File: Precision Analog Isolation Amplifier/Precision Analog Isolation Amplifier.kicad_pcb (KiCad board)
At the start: 2 copper layers, 33 parts, among them J1 Conn_01x03, J2 Conn_01x03, J3 Conn_Coaxial, J4 Conn_Coaxial

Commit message: Update Schematic & PCB
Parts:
- added C19: 0.1uF, Capacitor_SMD:C_0805_2012Metric_Pad1.18x1.45mm_HandSolder, F.Cu at (163.4, 94.2)
- added C20: 0.1uF, Capacitor_SMD:C_0805_2012Metric_Pad1.18x1.45mm_HandSolder, F.Cu at (167.6, 94.2)
- added D1: ---, Diode_SMD:D_0805_2012Metric_Pad1.15x1.40mm_HandSolder, F.Cu at (159.1, 94.1)
- added G***: LOGO, NaMi_logo:NaMi_logo, F.Cu at (124.9, 101.7)
- added IC1: ADA4899-1YRDZ, ADA4899:SOIC127P600X175-9N, F.Cu at (165.5, 90.3)
- added Q1: ---, Package_TO_SOT_SMD:SOT-23_Handsoldering, F.Cu at (154.9, 83.2)
- added R7: 50R, Resistor_SMD:R_0805_2012Metric_Pad1.20x1.40mm_HandSolder, F.Cu at (160.0, 100.3)
- added REF**: MountingHole_2.2mm_M2_Pad_Via, MountingHole:MountingHole_2.2mm_M2_Pad_Via, F.Cu at (125.6, 76.5)
- added REF**: MountingHole_2.2mm_M2_Pad_Via, MountingHole:MountingHole_2.2mm_M2_Pad_Via, F.Cu at (175.5, 111.5)
- added REF**: MountingHole_2.2mm_M2_Pad_Via, MountingHole:MountingHole_2.2mm_M2_Pad_Via, F.Cu at (175.4, 76.6)
- added REF**: MountingHole_2.2mm_M2_Pad_Via, MountingHole:MountingHole_2.2mm_M2_Pad_Via, F.Cu at (125.6, 111.5)
- added U1: HCNR201, HCNR201-300E:HCNR201300E, F.Cu at (149.8, 91.6)
- added U2: ADA4522, ADA4522:SOIC127P600X175-8N, F.Cu at (144.7, 101.1)
- added U4: ADA4522, ADA4522:SOIC127P600X175-8N, F.Cu at (136.5, 92.6)
- moved C9 76.9 mm to (162.5, 110.4), turned to 180 degrees
- moved C10 74.4 mm to (162.5, 108.4), turned to 180 degrees
- moved J2 73.4 mm to (152.3, 111.4), turned to -90 degrees
- moved C5 72.3 mm to (162.4, 83.7), turned to 180 degrees
- moved C11 72.1 mm to (162.5, 106.4), turned to 180 degrees
- moved C6 71.2 mm to (162.4, 81.7), turned to 180 degrees
- moved FB2 70.8 mm to (159.0, 79.1)
- moved C7 70.4 mm to (162.4, 79.7), turned to 180 degrees
- moved C12 70.0 mm to (162.5, 104.4), turned to 180 degrees
- moved C8 69.8 mm to (162.5, 77.7), turned to 180 degrees
- moved FB3 69.8 mm to (159.0, 109.1)
- moved R1 67.6 mm to (143.9, 84.0)
- moved J1 66.5 mm to (147.4, 76.7)
- moved R3 64.7 mm to (140.5, 88.6), turned to -90 degrees
- moved C17 61.1 mm to (137.4, 87.7), turned to 0 degrees
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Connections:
- C1 pad 2: Net-(C1-Pad2) -> VCC1 +15V
- C10 pad 2: Net-(C10-Pad2) -> VCC2 +15V
- C11 pad 2: Net-(C10-Pad2) -> VCC2 +15V
- C12 pad 2: Net-(C10-Pad2) -> VCC2 +15V
- C13 pad 2: Net-(C13-Pad2) -> VEE2 -15V
- C14 pad 2: Net-(C13-Pad2) -> VEE2 -15V
- C15 pad 2: Net-(C13-Pad2) -> VEE2 -15V
- C16 pad 2: Net-(C13-Pad2) -> VEE2 -15V
- C18 pad 1: Net-(J4-In) -> Vsep_out
- C2 pad 2: Net-(C1-Pad2) -> VCC1 +15V
- C3 pad 2: Net-(C1-Pad2) -> VCC1 +15V
- C4 pad 2: Net-(C1-Pad2) -> VCC1 +15V
- C5 pad 2: Net-(C5-Pad2) -> VEE1 -15V
- C6 pad 2: Net-(C5-Pad2) -> VEE1 -15V
- C7 pad 2: Net-(C5-Pad2) -> VEE1 -15V
- C8 pad 2: Net-(C5-Pad2) -> VEE1 -15V
- C9 pad 2: Net-(C10-Pad2) -> VCC2 +15V
- FB1 pad 1: VCC1 +15V -> VCC1 IN +15V
- FB1 pad 2: Net-(C1-Pad2) -> VCC1 +15V
- FB2 pad 1: VEE1 -15V -> VEE1 IN -15V
- FB2 pad 2: Net-(C5-Pad2) -> VEE1 -15V
- FB3 pad 1: VCC2 +15V -> VCC2 IN +15V
- FB3 pad 2: Net-(C10-Pad2) -> VCC2 +15V
- FB4 pad 1: VEE2 -15V -> VEE2 IN -15V
- FB4 pad 2: Net-(C13-Pad2) -> VEE2 -15V
- J1 pad 1: VCC1 +15V -> VCC1 IN +15V
- J1 pad 3: VEE1 -15V -> VEE1 IN -15V
- J2 pad 1: VCC2 +15V -> VCC2 IN +15V
- J2 pad 3: VEE2 -15V -> VEE2 IN -15V
- J4 pad 1: Net-(J4-In) -> Vout
- RV1 pad 1: Net-(J4-In) -> Vsep_out
- RV1 pad 2: Net-(J4-In) -> Vsep_out
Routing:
- net GND1: track 0.00 -> 122.1 mm, vias 0 -> 7
- net GND2: track 0.00 -> 118.0 mm, vias 0 -> 4
- net VEE1 -15V: track 0.00 -> 51.3 mm, vias 0 -> 2
- net VCC2 +15V: track 0.00 -> 48.8 mm, vias 0 -> 6
- net VEE2 -15V: track 0.00 -> 43.3 mm, vias 0 -> 2
- net VCC1 +15V: track 0.00 -> 34.9 mm, vias 0 -> 2
- net Net-(U1B-K): track 0.00 -> 33.8 mm, vias 0 -> 2
- net Net-(D1-K): track 0.00 -> 29.6 mm
- net Vsep_out: track 0.00 -> 26.5 mm
- net Net-(U1C-K): track 0.00 -> 21.9 mm, vias 0 -> 2
- net Net-(Q1-B): track 0.00 -> 21.3 mm, vias 0 -> 2
- net Vout: track 0.00 -> 18.4 mm, vias 0 -> 2
- net Net-(R6-Pad2): track 0.00 -> 11.4 mm
- net Net-(IC1-+IN): track 0.00 -> 9.94 mm
- net Net-(J3-In): track 0.00 -> 7.24 mm
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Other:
- board outline added: 56 x 41 mm
- board text added: "Input"
- board text added: "KN NaMi Precision Analog Isolation Amplifier Adam Matysiak Kacper Kowalik"
- board text added: "Output"
- board text added: "Primary power supply input"
- board text added: "Secondary power supply input"

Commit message: Update PCB
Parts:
- removed REF** (x4): MountingHole_2.2mm_M2_Pad_Via, MountingHole:MountingHole_2.2mm_M2_Pad_Via
- added D2: SMAJ15A, Diode_SMD:D_SMA, F.Cu at (102.5, 98.0)
- added D3: SMAJ15A, Diode_SMD:D_SMA, F.Cu at (102.5, 77.5)
- added D4: SMAJ15A, Diode_SMD:D_SMA, F.Cu at (175.1, 97.0)
- added D5: SMAJ15A, Diode_SMD:D_SMA, F.Cu at (175.1, 77.0)
- added D6: LED, Diode_SMD:D_0805_2012Metric_Pad1.15x1.40mm_HandSolder, F.Cu at (105.5, 82.0)
- added D7: LED, Diode_SMD:D_0805_2012Metric_Pad1.15x1.40mm_HandSolder, F.Cu at (105.0, 94.0)
- added D8: LED, Diode_SMD:D_0805_2012Metric_Pad1.15x1.40mm_HandSolder, F.Cu at (172.1, 92.5)
- added D9: LED, Diode_SMD:D_0805_2012Metric_Pad1.15x1.40mm_HandSolder, F.Cu at (172.1, 81.5)
- added F1: Fuse, Resistor_SMD:R_0805_2012Metric_Pad1.20x1.40mm_HandSolder, F.Cu at (101.0, 90.5)
- added F2: Fuse, Resistor_SMD:R_0805_2012Metric_Pad1.20x1.40mm_HandSolder, F.Cu at (101.0, 84.5)
- added F3: Fuse, Resistor_SMD:R_0805_2012Metric_Pad1.20x1.40mm_HandSolder, F.Cu at (176.6, 84.0)
- added F4: Fuse, Resistor_SMD:R_0805_2012Metric_Pad1.20x1.40mm_HandSolder, F.Cu at (176.6, 90.0)
- added R10: 33k, Resistor_SMD:R_0805_2012Metric_Pad1.20x1.40mm_HandSolder, F.Cu at (176.6, 92.5)
- added R11: 33k, Resistor_SMD:R_0805_2012Metric_Pad1.20x1.40mm_HandSolder, F.Cu at (176.6, 81.5)
- added R8: 33k, Resistor_SMD:R_0805_2012Metric_Pad1.20x1.40mm_HandSolder, F.Cu at (101.0, 82.0)
- added R9: 33k, Resistor_SMD:R_0805_2012Metric_Pad1.20x1.40mm_HandSolder, F.Cu at (100.5, 94.0)
- moved C8 55.8 mm to (110.0, 96.5)
- moved FB2 54.6 mm to (105.6, 90.5), turned to 0 degrees
- moved C7 54.5 mm to (110.0, 94.5)
- moved C6 53.6 mm to (110.0, 92.5)
- moved C5 52.9 mm to (110.0, 90.5)
- moved J1 51.5 mm to (96.5, 85.0), turned to 0 degrees
- moved J2 39.5 mm to (181.1, 84.5), turned to 0 degrees
- moved Q1 38.0 mm to (117.0, 85.5)
- moved FB4 36.3 mm to (171.6, 90.0), turned to 180 degrees
- moved FB1 35.5 mm to (105.6, 84.5), turned to 0 degrees
- moved C13 33.1 mm to (167.1, 90.0)
- moved C14 33.1 mm to (167.1, 92.0)
- moved C15 33.1 mm to (167.1, 94.0)
- moved C16 33.0 mm to (167.1, 96.2)
- moved C9 32.7 mm to (167.1, 78.0), turned to 0 degrees
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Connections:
- J1 pad 1: VCC1 IN +15V -> Net-(J1-Pin_1)
- J1 pad 3: VEE1 IN -15V -> Net-(J1-Pin_3)
- J2 pad 1: VCC2 IN +15V -> Net-(J2-Pin_1)
- J2 pad 3: VEE2 IN -15V -> Net-(J2-Pin_3)
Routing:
- net GND2: track 118.0 -> 13.1 mm, vias 4 -> 0
- net GND1: track 122.1 -> 70.1 mm, vias 7 -> 0
- net VEE1 -15V: track 51.3 -> 2.95 mm, vias 2 -> 0
- net VCC2 +15V: track 48.8 -> 12.4 mm, vias 6 -> 0
- net VEE2 -15V: track 43.3 -> 10.9 mm, vias 2 -> 0
- net Net-(C17-Pad2): track 4.42 -> 26.5 mm, vias 0 -> 2
- net Net-(Q1-B): track 21.3 -> 6.60 mm, vias 2 -> 0
- net Net-(D1-K): track 29.6 -> 14.9 mm
- net Vout: track 18.4 -> 7.35 mm, vias 2 -> 0
- net Net-(Q1-E): track 5.03 -> 13.8 mm
- net Net-(U1B-K): track 33.8 -> 25.8 mm
- net Net-(J3-In): track 7.24 -> 0.00 mm
- net VCC1 IN +15V: track 7.00 -> 0.00 mm
- net VCC2 IN +15V: track 6.98 -> 0.00 mm
- net VEE1 IN -15V: track 6.89 -> 0.00 mm
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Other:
- board outline removed
- board text removed: "+15V"
- board text removed: "-15V"
- board text removed: "GND1"
- board text removed: "GND2"
- board text removed: "Input"
- board text removed: "Output"
- board text removed: "Primary power supply input"
- board text removed: "Secondary power supply input"

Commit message: Update PCB layout
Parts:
- added REF**: MountingHole_2.2mm_M2_DIN965_Pad, MountingHole:MountingHole_2.2mm_M2_DIN965_Pad, F.Cu at (171.2, 117.3)
- added REF**: MountingHole_2.2mm_M2_DIN965_Pad, MountingHole:MountingHole_2.2mm_M2_DIN965_Pad, F.Cu at (171.2, 79.3)
- added REF**: MountingHole_2.2mm_M2_DIN965_Pad, MountingHole:MountingHole_2.2mm_M2_DIN965_Pad, F.Cu at (113.7, 79.3)
- added REF**: MountingHole_2.2mm_M2_DIN965_Pad, MountingHole:MountingHole_2.2mm_M2_DIN965_Pad, F.Cu at (113.7, 117.3)
- moved R2 39.3 mm to (132.0, 112.8), turned to 90 degrees
- moved R1 36.3 mm to (130.1, 112.8), turned to 90 degrees
- moved U4 35.1 mm to (135.8, 110.8), turned to -90 degrees
- moved R3 33.4 mm to (128.2, 112.8), turned to -90 degrees
- moved RV1 33.3 mm to (147.3, 109.1), turned to -90 degrees
- moved Q1 26.9 mm to (130.1, 109.0), turned to 0 degrees
- moved R5 26.9 mm to (129.3, 106.2), turned to 0 degrees
- moved D1 24.9 mm to (125.3, 108.2), turned to 180 degrees
- moved C17 23.9 mm to (126.2, 112.8), turned to -90 degrees
- moved R6 22.6 mm to (152.9, 111.0)
- moved D3 20.3 mm to (122.0, 83.0), turned to 180 degrees
- moved R9 20.1 mm to (120.3, 97.3)
- moved C5 20.0 mm to (129.4, 95.1)
- moved C6 20.0 mm to (129.4, 97.1)
- moved C7 20.0 mm to (129.4, 99.1)
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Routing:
- net GND1: track 70.1 -> 0.00 mm
- net VCC1 +15V: track 38.3 -> 0.00 mm
- net Vsep_out: track 28.4 -> 0.00 mm, vias 2 -> 0
- net Net-(C17-Pad2): track 26.5 -> 0.00 mm, vias 2 -> 0
- net Net-(U1B-K): track 25.8 -> 0.00 mm, vias 2 -> 0
- net Net-(U1C-K): track 17.2 -> 0.00 mm
- net Net-(D1-K): track 14.9 -> 0.00 mm
- net Net-(R6-Pad2): track 14.2 -> 0.00 mm
- net Net-(Q1-E): track 13.8 -> 0.00 mm
- net GND2: track 13.1 -> 0.00 mm
- net VCC2 +15V: track 12.4 -> 0.00 mm
- net VEE2 -15V: track 10.9 -> 0.00 mm
- net Net-(IC1-+IN): track 10.0 -> 0.00 mm, vias 2 -> 0
- net Vout: track 7.35 -> 0.00 mm
- net Net-(Q1-B): track 6.60 -> 0.00 mm
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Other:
- board outline added: 63.5 x 44 mm

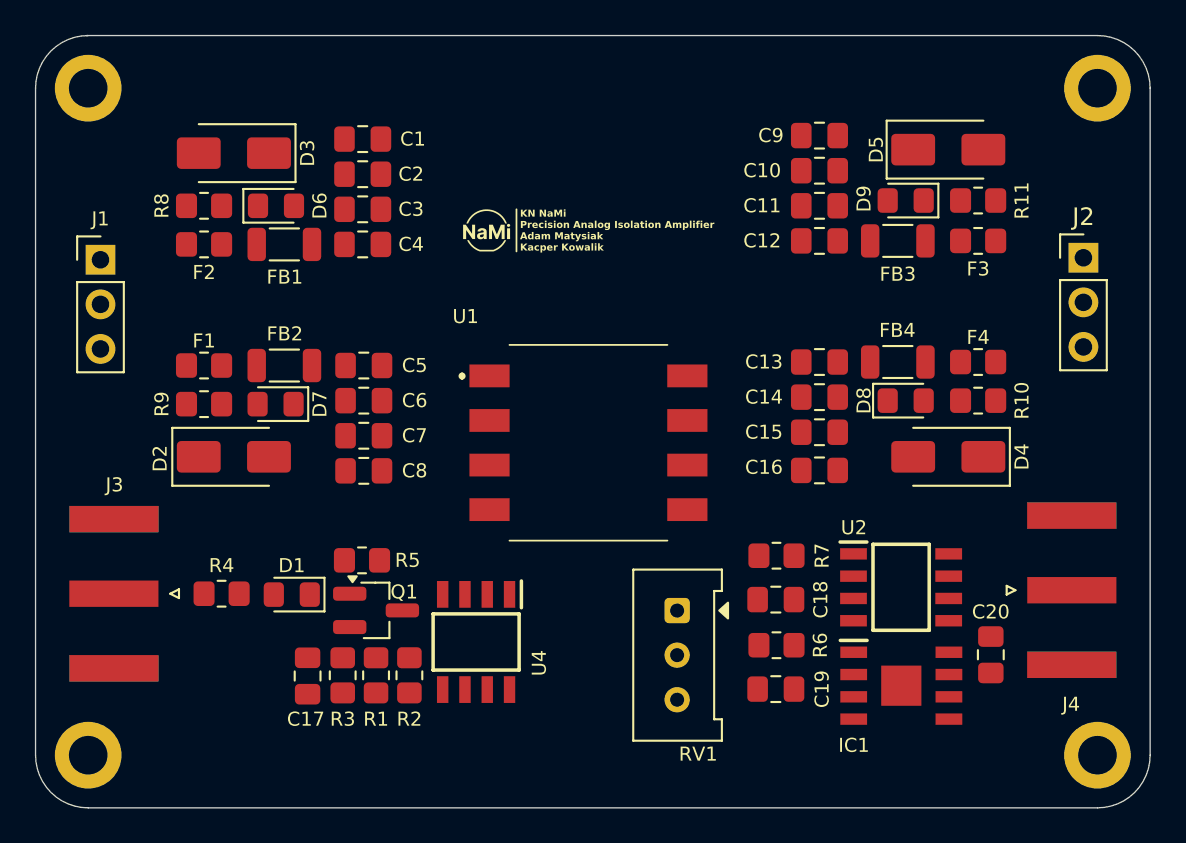
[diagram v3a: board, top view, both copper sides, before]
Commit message: Update Schematic and Add Tracks to PCB
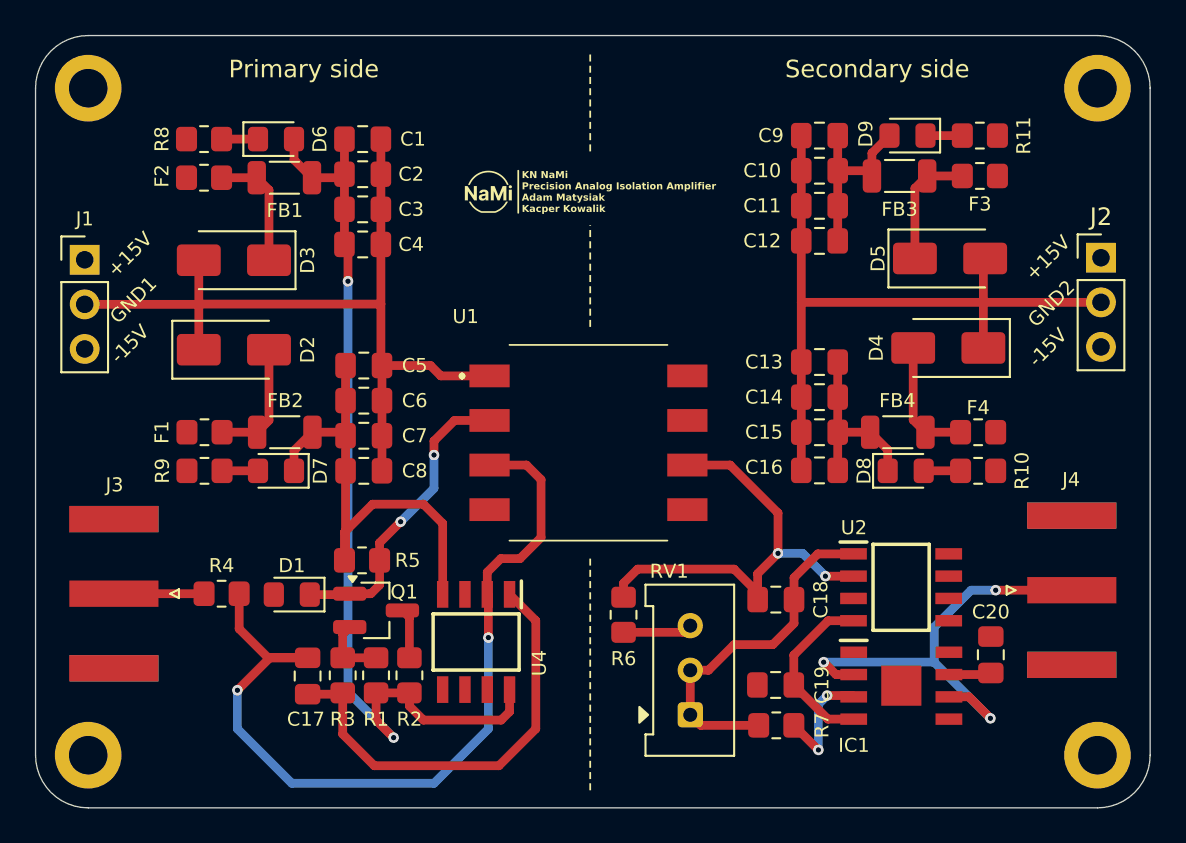
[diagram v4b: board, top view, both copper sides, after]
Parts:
- moved R7 9.67 mm to (152.9, 115.6)
- moved R6 8.88 mm to (144.2, 109.3), turned to -90 degrees
- moved D5 6.20 mm to (162.8, 89.0)
- moved D4 6.20 mm to (162.7, 94.1)
- moved D2 6.10 mm to (122.0, 94.2)
- moved D3 6.10 mm to (122.0, 89.1)
- moved RV1 5.99 mm to (148.0, 115.0), turned to 90 degrees
- moved D8 4.00 mm to (160.3, 101.1)
- moved F4 4.00 mm to (164.4, 98.9)
- moved FB4 4.00 mm to (159.8, 98.9)
- moved R10 4.00 mm to (164.4, 101.1)
- moved F1 3.80 mm to (120.3, 98.9)
- moved FB2 3.80 mm to (124.9, 98.9)
- moved D7 3.80 mm to (124.4, 101.1)
- moved R9 3.80 mm to (120.3, 101.1)
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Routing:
- net VCC1 +15V: track 0.00 -> 52.9 mm, vias 0 -> 2
- net Net-(U1B-K): track 0.00 -> 49.8 mm, vias 0 -> 2
- net GND1: track 0.00 -> 47.3 mm
- net GND2: track 0.00 -> 41.2 mm
- net VEE1 -15V: track 0.00 -> 28.1 mm
- net Vout: track 0.00 -> 26.4 mm, vias 0 -> 3
- net Net-(U1C-K): track 0.00 -> 26.3 mm, vias 0 -> 2
- net Net-(C17-Pad2): track 0.00 -> 25.3 mm
- net VEE2 -15V: track 0.00 -> 20.8 mm
- net Vsep_out: track 0.00 -> 20.3 mm
- net Net-(D1-K): track 0.00 -> 17.3 mm, vias 0 -> 2
- net VCC2 +15V: track 0.00 -> 13.2 mm
- net VEE2 IN -15V: track 0.00 -> 7.09 mm
- net VCC2 IN +15V: track 0.00 -> 6.99 mm
- net VCC1 IN +15V: track 0.00 -> 6.99 mm
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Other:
- outline, holes or cut-outs redrawn
- board text added: "+15V"
- board text added: "-15V"
- board text added: "GND1"
- board text added: "GND2"
- board text added: "Primary side"
- board text added: "Secondary side"

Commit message: update pcb
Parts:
- J3, J4: footprint Connector_Coaxial:SMA_Amphenol_132289_EdgeMount -> CONN SMA JACK STR 50 OHM SMD:CONN_732511350_MOL
- moved R6 5.13 mm to (147.0, 105.0), turned to 180 degrees
- moved U1 2.50 mm to (142.2, 97.0)
- moved R4 1.90 mm to (121.3, 110.0)
- moved C20 1.65 mm to (166.0, 113.0), turned to 180 degrees
- moved J4 0.39 mm to (170.1, 107.9)
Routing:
- net GND2: track 41.2 -> 117.3 mm, vias 0 -> 6
- net GND1: track 47.3 -> 111.4 mm, vias 0 -> 8
- net VCC2 +15V: track 13.2 -> 42.7 mm, vias 0 -> 2
- net VEE2 -15V: track 20.8 -> 30.7 mm, vias 0 -> 2
- net Net-(J2-Pin_3): track 0.00 -> 8.01 mm
- net Net-(J2-Pin_1): track 0.00 -> 7.83 mm
- net Net-(J1-Pin_3): track 0.00 -> 7.79 mm
- net Net-(J1-Pin_1): track 0.00 -> 7.74 mm
- net Net-(D1-K): track 17.3 -> 20.0 mm
- net Net-(R6-Pad2): track 3.96 -> 6.29 mm
- net Net-(U1C-K): track 26.3 -> 24.9 mm
- net Net-(J3-In): track 5.14 -> 5.92 mm
- net Net-(U1B-K): track 49.8 -> 49.4 mm, vias 2 -> 4
